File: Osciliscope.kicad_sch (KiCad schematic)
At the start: 20 parts, among them J1 USB_C_Receptacle_USB2.0_14P, U1 STM32H753VITx, X1 X322525MOB4SI

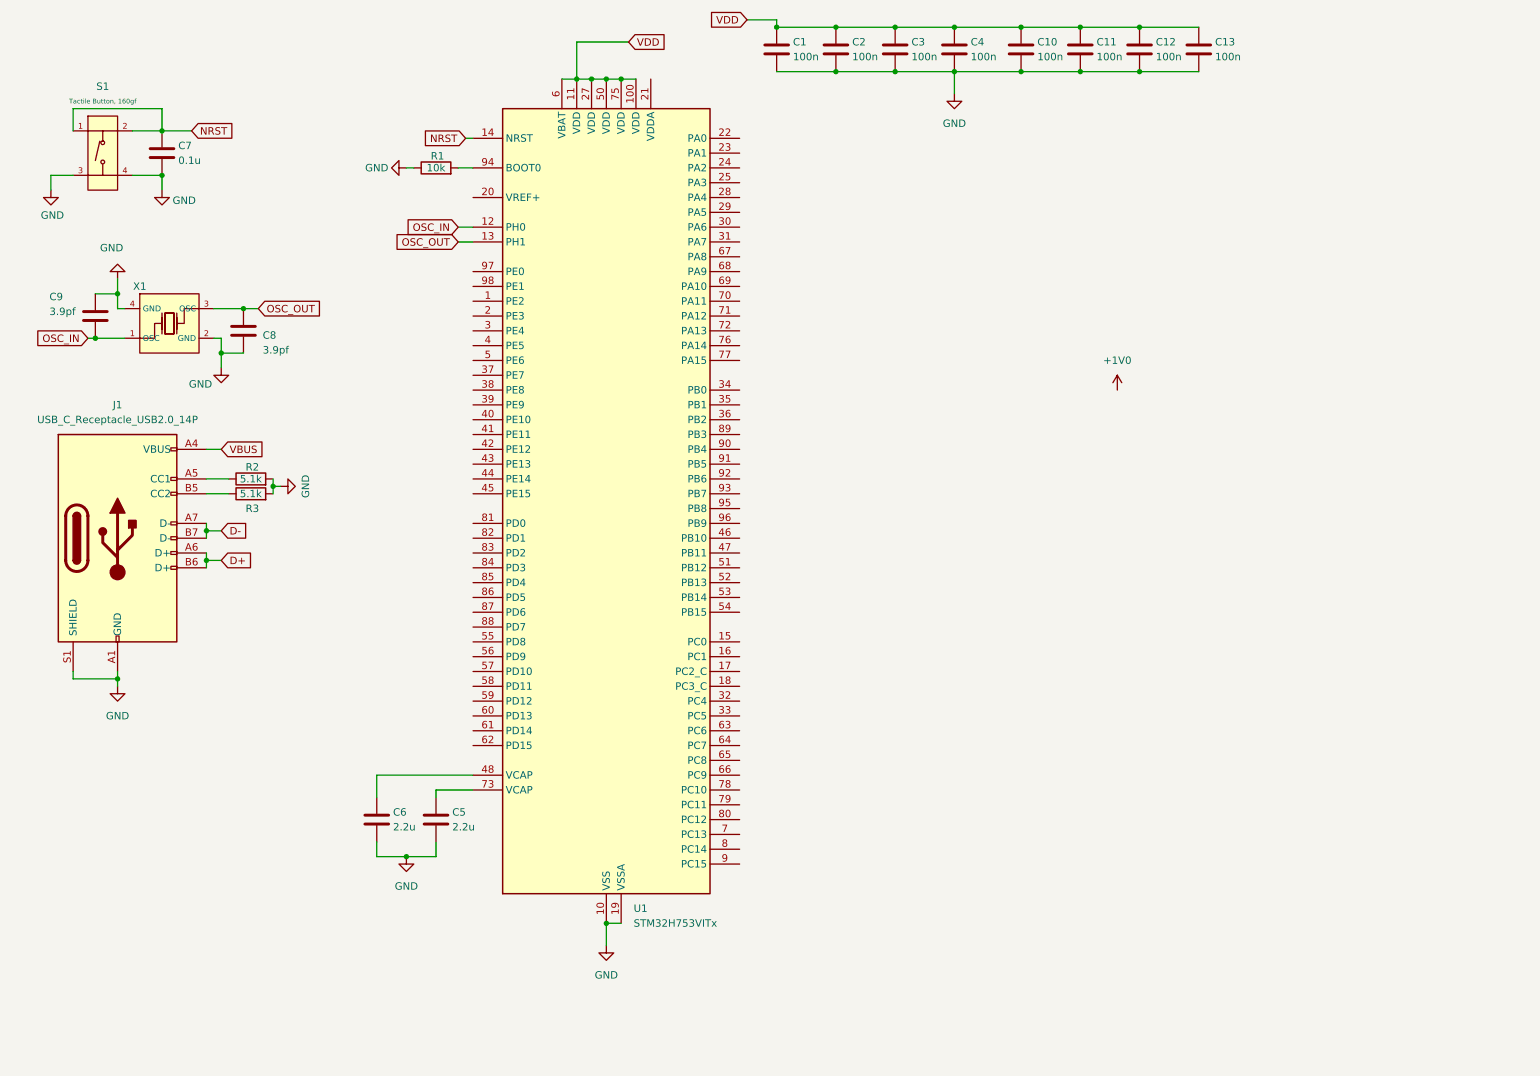
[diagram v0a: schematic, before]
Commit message: Labelled some stuff
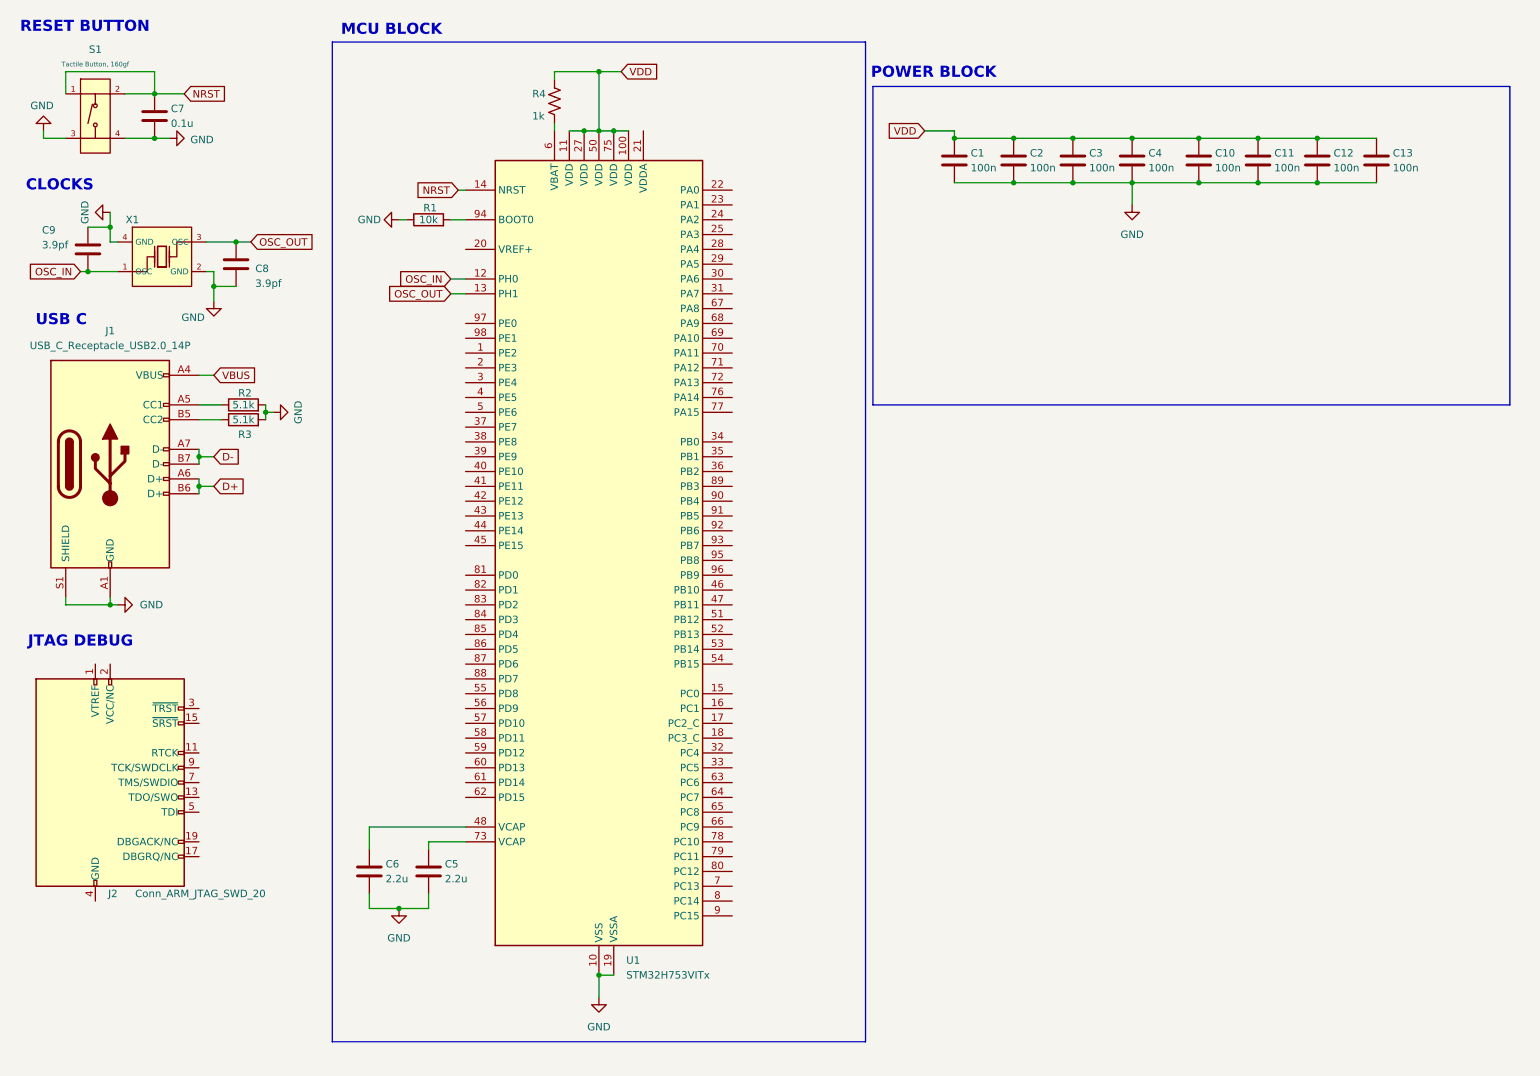
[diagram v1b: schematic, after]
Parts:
- added J2: Conn_ARM_JTAG_SWD_20, Connector_PinSocket_2.54mm:PinSocket_2x10_P2.54mm_Vertical, symbol Connector:Conn_ARM_JTAG_SWD_20
- added R4: 1k, Resistor_SMD:R_0603_1608Metric, symbol Device:R_US
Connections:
- net VDD: now also R4.1; no longer U1.6 (VBAT)
- new net: R4.2, U1.6 (VBAT)
- new net: J2.10 (GND), J2.12 (GND), J2.14 (GND), J2.16 (GND), J2.18 (GND), J2.20 (GND), J2.4 (GND), J2.6 (GND), J2.8 (GND)
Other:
- note added: "CLOCKS"
- note added: "JTAG DEBUG"
- note added: "MCU BLOCK"
- note added: "POWER BLOCK"
- note added: "RESET BUTTON"
- note added: "USB C"
- moved on the sheet: C1, C10, C11, C12, C13, C2, C3, C4, C5, C6, C7, C8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

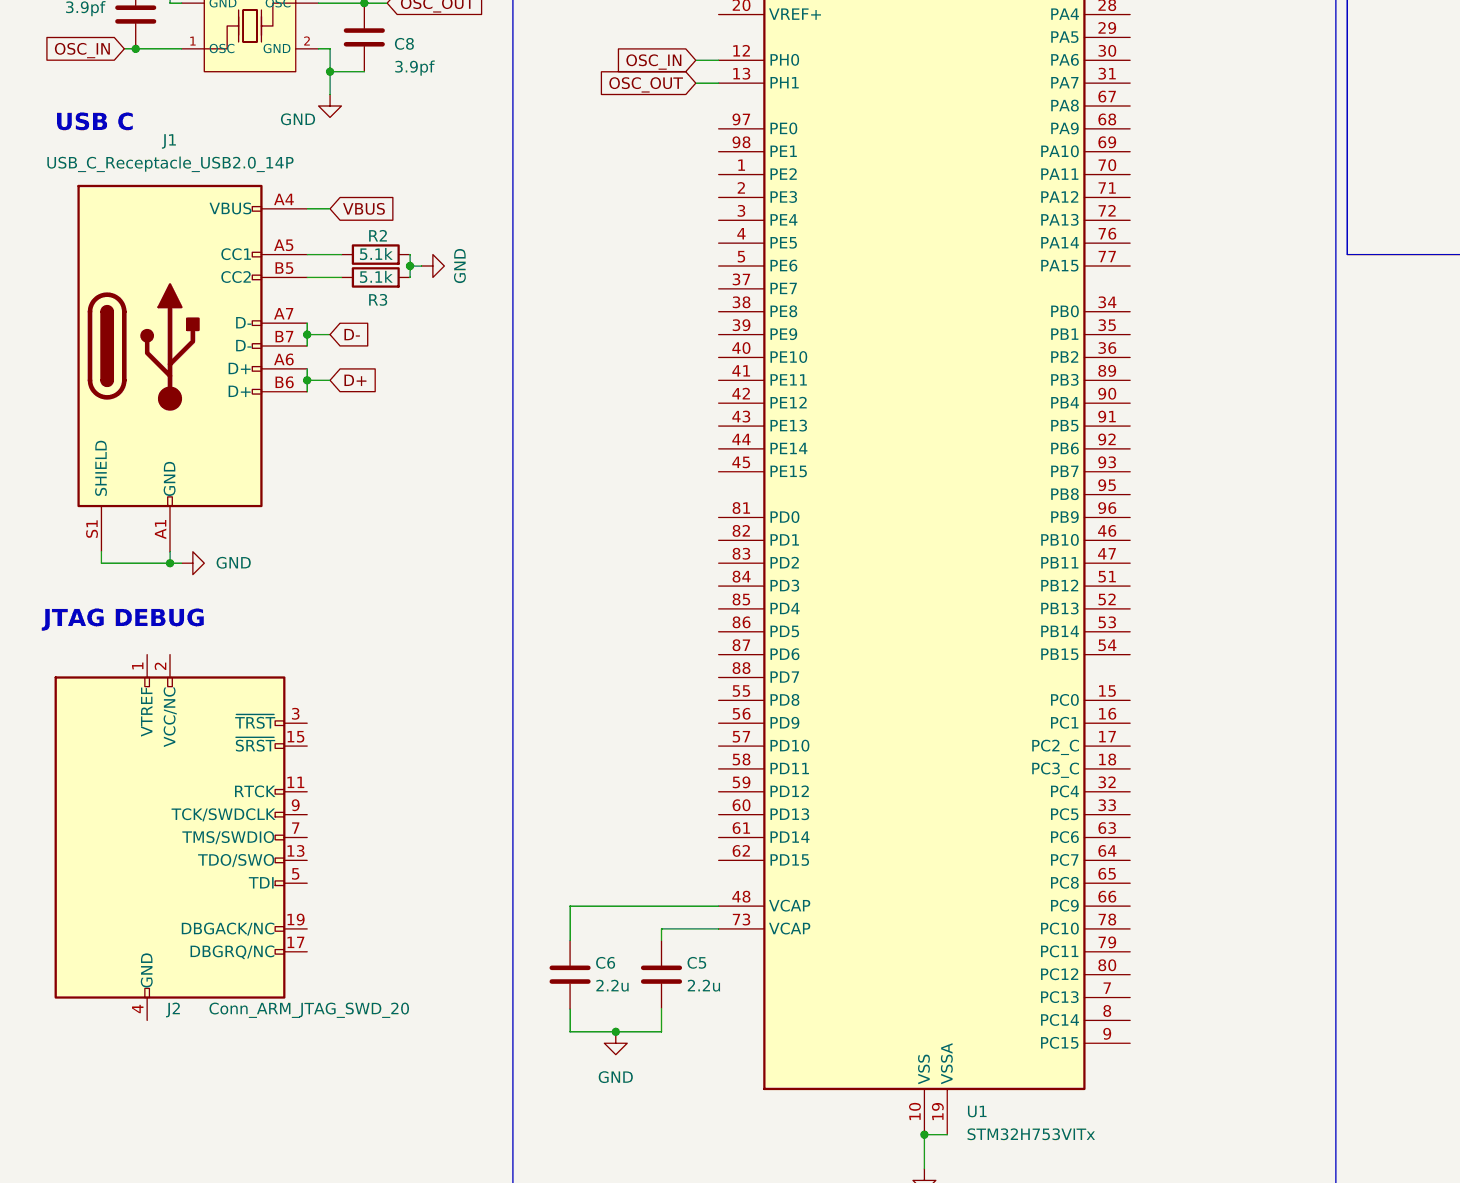
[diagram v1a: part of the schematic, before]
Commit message: Added USB and SWD
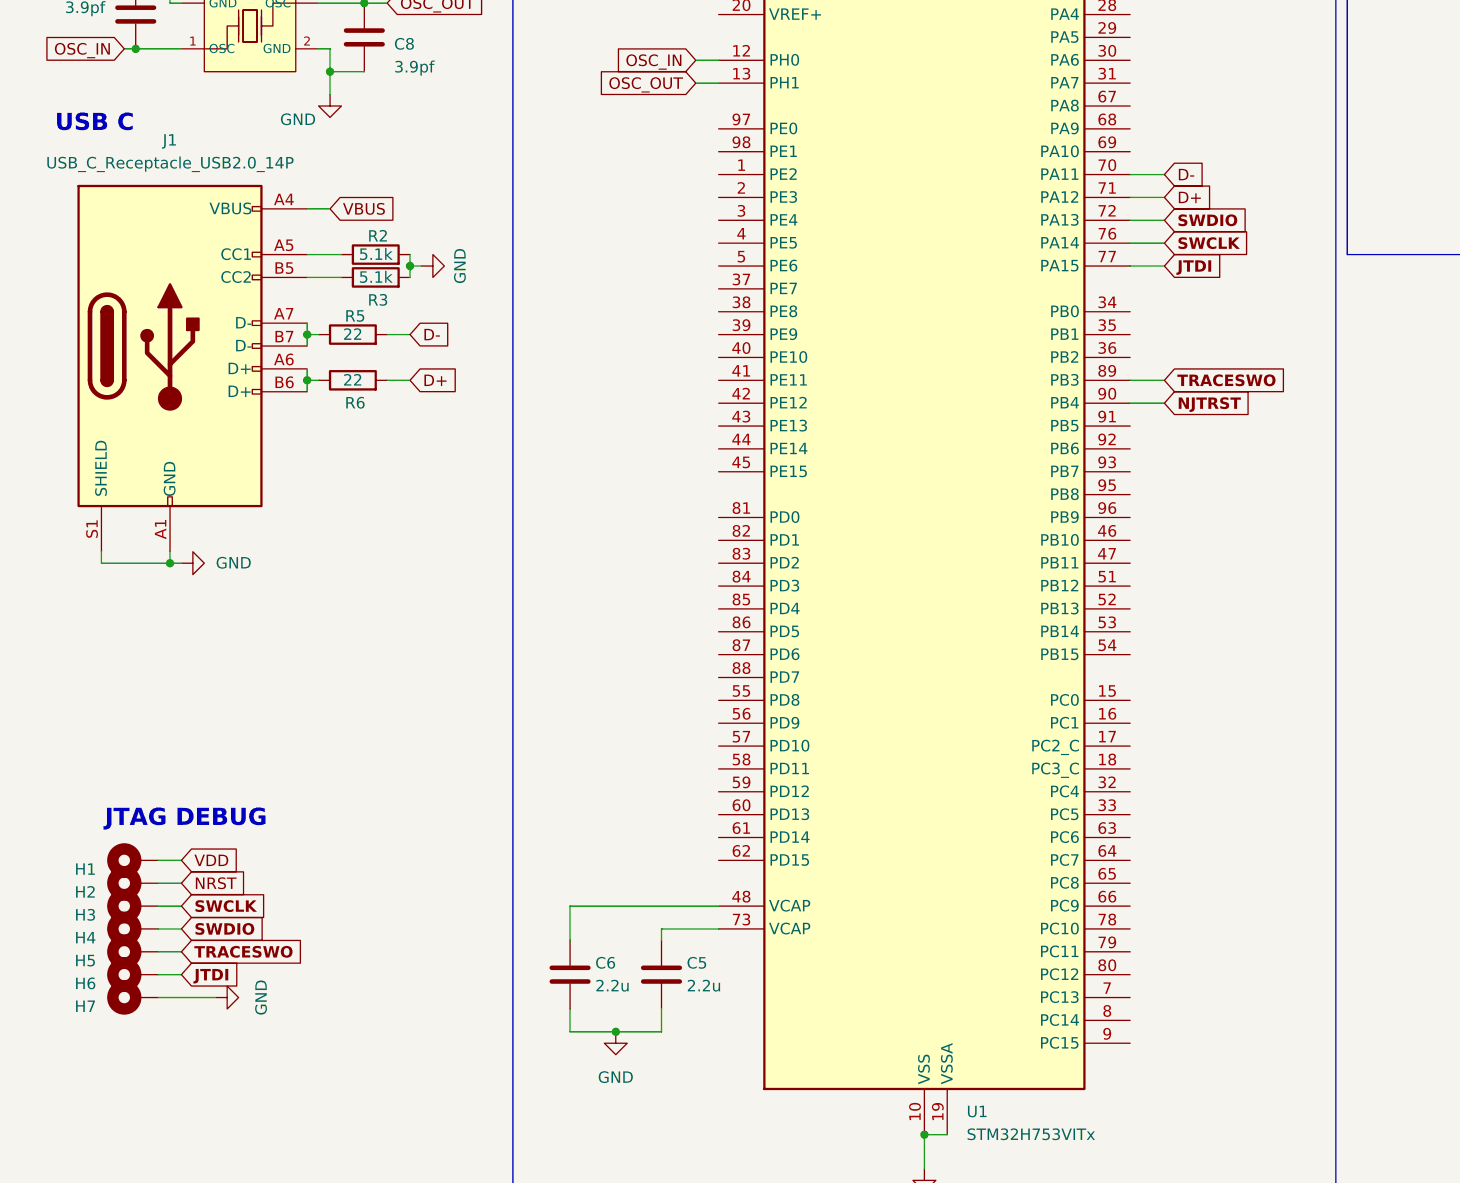
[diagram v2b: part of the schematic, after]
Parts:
- removed J2: Conn_ARM_JTAG_SWD_20, Connector_PinSocket_2.54mm:PinSocket_2x10_P2.54mm_Vertical, symbol Connector:Conn_ARM_JTAG_SWD_20
- added H1, H2, H3, H4, H5, H6, H7: MountingHole_Pad, symbol Mechanical:MountingHole_Pad
- added R5, R6: 22, symbol Device:R
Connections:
- net D+: now also U1.71 (PA12), R6.2; no longer J1.A6 (D+), J1.B6 (D+)
- net D-: now also U1.70 (PA11), R5.2; no longer J1.A7 (D-), J1.B7 (D-)
- net GND: now also H7.1
- net NRST: now also H2.1
- net VDD: now also H1.1
- net SWDIO: now reaches U1.72 (PA13)
- net SWDIO: now also H4.1
- net SWCLK: now reaches U1.76 (PA14)
- net SWCLK: now also H3.1
- net JTDI: now reaches U1.77 (PA15)
- net JTDI: now also H6.1
- net TRACESWO: now reaches U1.89 (PB3)
- net TRACESWO: now also H5.1
- net NJTRST: now reaches U1.90 (PB4)
- new net: J1.A6 (D+), J1.B6 (D+), R6.1
- new net: J1.A7 (D-), J1.B7 (D-), R5.1

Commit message: Brick all of it
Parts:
- removed C1, C10, C11, C12, C13, C2, C3, C4: 100n, symbol Device:C
- removed C5, C6: 2.2u, symbol Device:C
- removed C7: 0.1u, symbol Device:C
- removed C8, C9: 3.9pf, symbol Device:C
- removed H1, H2, H3, H4, H5, H6, H7: MountingHole_Pad, symbol Mechanical:MountingHole_Pad
- removed J1: USB_C_Receptacle_USB2.0_14P, symbol Connector:USB_C_Receptacle_USB2.0_14P
- removed R2, R3: 5.1k, symbol Device:R
- removed R4: 1k, Resistor_SMD:R_0603_1608Metric, symbol Device:R_US
- removed S1: Tactile Button, 160gf, PCM_JLCPCB:SW-SMD_4P-L5.1-W5.1-P3.70-LS6.5-TL-2, symbol PCM_JLCPCB-Connectors_Buttons:Tactile Button, 160gf, 12V, 50mA, 5.1mm
- removed U1: STM32H753VITx, Package_QFP:LQFP-100_14x14mm_P0.5mm, symbol MCU_ST_STM32H7:STM32H753VITx
- removed X1: X322525MOB4SI, PCM_JLCPCB:OSC-SMD_4P-L3.2-W2.5-BL, symbol PCM_JLCPCB-Crystals:Crystal, 25MHz, 11pF
- added J1, J2: U.FL, PCM_JLCPCB:IPEX-SMD_BWIPX-1-001E, symbol PCM_JLCPCB-Extended:RF, Connector, U.FL
- added J3, J4: Conn_01x20_Socket, symbol Connector:Conn_01x20_Socket
- added R4: 1M, symbol Device:R
- added SW1, SW2: SW_Rotary_1x8_MP, symbol Switch:SW_Rotary_1x8_MP
- added U3: MAX19777AZA_T, MAX19777AZA_T:BGA8N35P2X4_85X143X37N, symbol MAX19777AZA_T:MAX19777AZA_T
- added U4: LM358, symbol Amplifier_Operational:LM358
- R1: value 10k -> 1M
- R5, R6: value 22 -> 1M
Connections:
- net D- is gone; now on an unnamed net: R5.2
- net GND: now also R1.2, J1.2 (Ext), R4.2; no longer R1.1
- net RAW_IN_1: now reaches R6.1
- net RAW_IN_1: now also R1.1, J1.1 (In)
- net CHAN_1: now reaches R5.1
- net CHAN_1: now also U4.1
- net D+: no longer names the net of R6.2
- net D+: now also U4.2 (-)
- new net: R4.1, U4.3 (+)
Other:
- note removed: "CLOCKS"
- note removed: "JTAG DEBUG"
- note removed: "MCU BLOCK"
- note removed: "POWER BLOCK"
- note removed: "RESET BUTTON"
- note removed: "USB C"

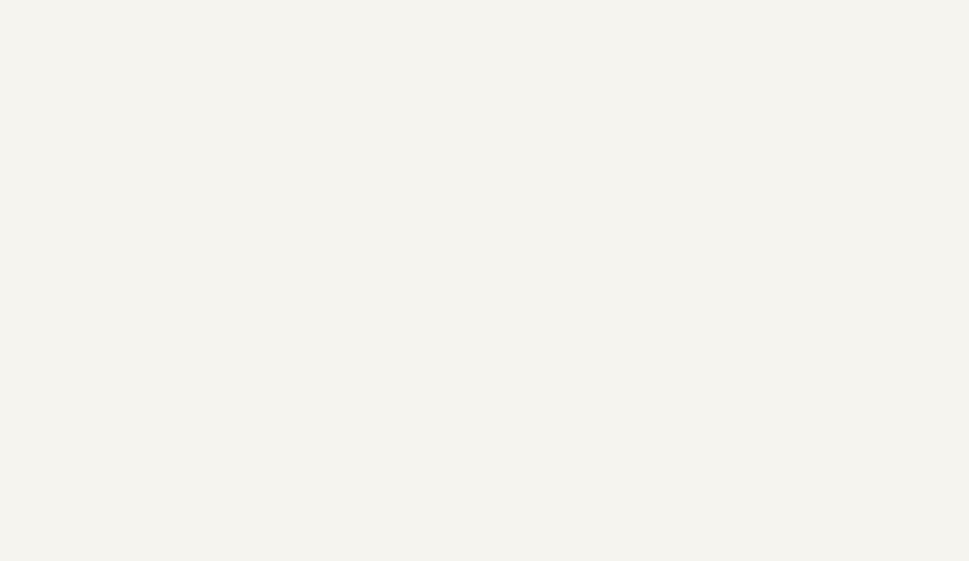
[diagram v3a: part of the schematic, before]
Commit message: Added LDO with cap filtering
This is what I think will work for our application since we don't need to run very much off of it
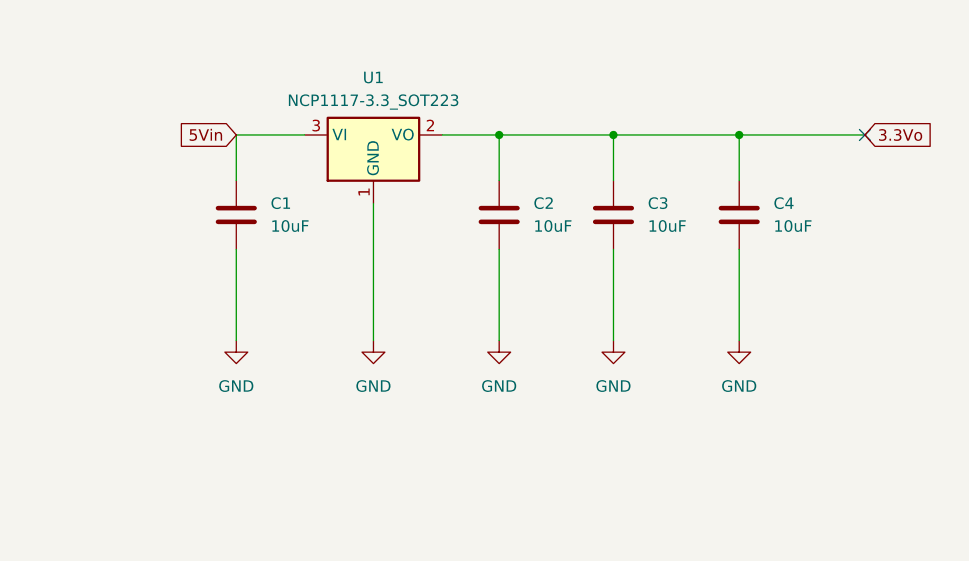
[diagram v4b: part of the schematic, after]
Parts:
- added C1, C2, C3, C4: 10uF, Capacitor_SMD:C_1206_3216Metric, symbol Device:C
- added U1: NCP1117-3.3_SOT223, Package_TO_SOT_SMD:SOT-223-3_TabPin2, symbol Regulator_Linear:NCP1117-3.3_SOT223
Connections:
- net GND: now also C1.2, C2.2, C3.2, C4.2, U1.1 (GND)
- new net 3.3Vo: C2.1, C3.1, C4.1, U1.2 (VO)
- new net 5Vin: C1.1, U1.3 (VI)
- no-connect marks 0 -> 1

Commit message: updated volt reg
updated volt reg
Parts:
- removed U1: NCP1117-3.3_SOT223, Package_TO_SOT_SMD:SOT-223-3_TabPin2, symbol Regulator_Linear:NCP1117-3.3_SOT223
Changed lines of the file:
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@@
-	)
-	(symbol
-		(lib_id "Regulator_Linear:NCP1117-3.3_SOT223")
-		(at 208.28 41.91 0)
-		(unit 1)
-		(exclude_from_sim no)
-		(in_bom yes)
-		(on_board yes)
-		(dnp no)
-		(fields_autoplaced yes)
-		(property "Reference" "U1"
-			(at 208.28 35.56 0)
-			(effects
-				(font
-					(size 1.27 1.27)
-				)
-			)
-		)
-		(property "Value" "NCP1117-3.3_SOT223"
-			(at 208.28 38.1 0)
-			(effects
-				(font
-					(size 1.27 1.27)
-				)
-			)
-		)
-		(property "Footprint" "Package_TO_SOT_SMD:SOT-223-3_TabPin2"
-			(at 208.28 36.83 0)
-			(effects
-				(font
-					(size 1.27 1.27)
-				)
-				(hide yes)
-			)
-		)
-		(property "Datasheet" "http://www.onsemi.com/pub_link/Collateral/NCP1117-D.PDF"
-			(at 210.82 48.26 0)
-			(effects
-				(font
-					(size 1.27 1.27)
-				)
-				(hide yes)
-			)
-		)
-		(property "Description" "1A Low drop-out regulator, Fixed Output 3.3V, SOT-223"
-			(at 208.28 41.91 0)
-			(effects
-				(font
-					(size 1.27 1.27)
-				)
-				(hide yes)
-			)
-		)
-		(pin "3"
-		)
-		(pin "1"
-		)
-		(pin "2"
-		)
-		(instances
-			(project ""
-				(path "/8c683ef5-a777-4de0-90bd-818351a6a189"
-					(reference "U1")
-					(unit 1)
-				)
-			)
-		)
 	)
 	(symbol

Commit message: updates to volt reg again
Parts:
- removed C3, C4: 10uF, Capacitor_SMD:C_1206_3216Metric, symbol Device:C
- added U1: MCP1700x-330xxMB, Package_TO_SOT_SMD:SOT-89-3, symbol Regulator_Linear:MCP1700x-330xxMB
- C1, C2: value 10uF -> 1uF
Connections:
- net 3.3Vo: now also U1.3 (VO)
- net 5Vin: now also U1.2 (VI)
- net GND: now also U1.1 (GND)
- no-connect marks 1 -> 0
